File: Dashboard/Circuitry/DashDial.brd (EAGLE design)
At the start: 88.9 x 66.3 mm, 32 parts, among them IC1 TLC5947DAPR, U1 LOGIC SHIFTER, X1 DIAL_IN, X2 SERVO

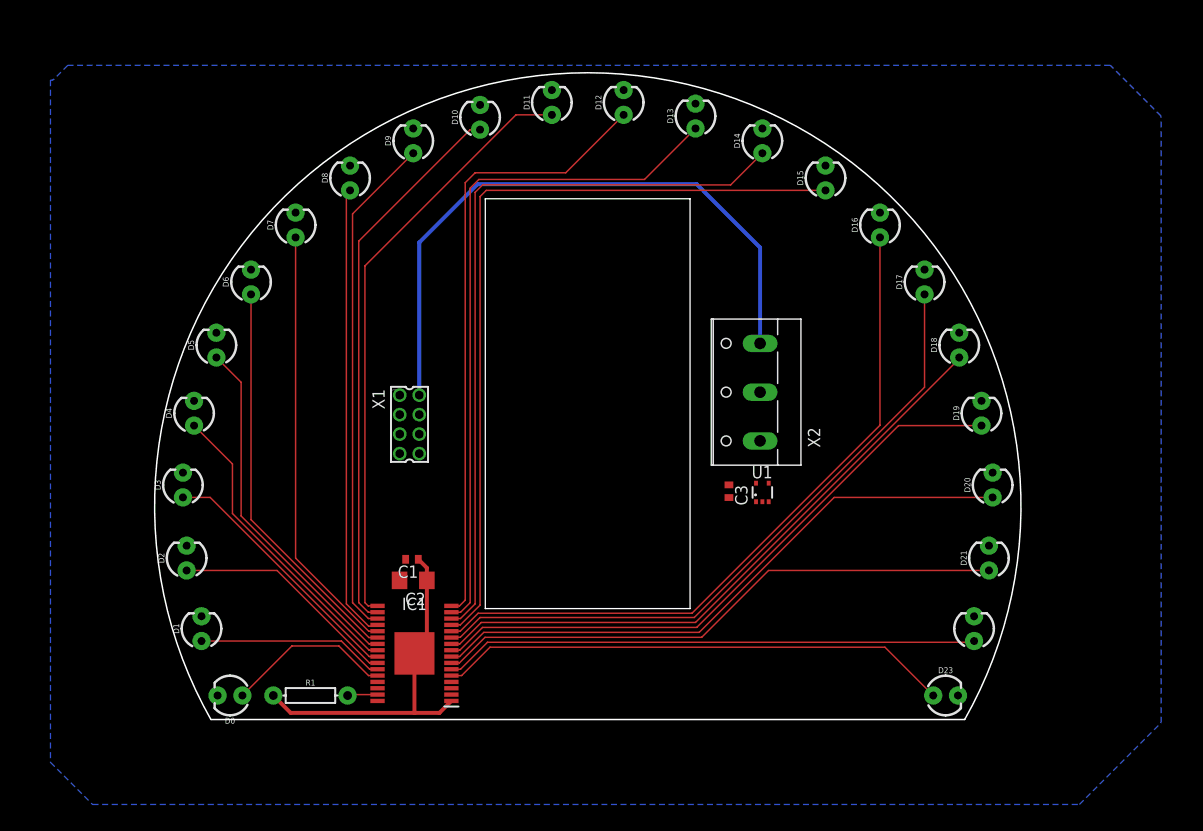
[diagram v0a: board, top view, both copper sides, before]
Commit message: Finished dashboard PCB's! Can send to JLC on Friday. @Andrew
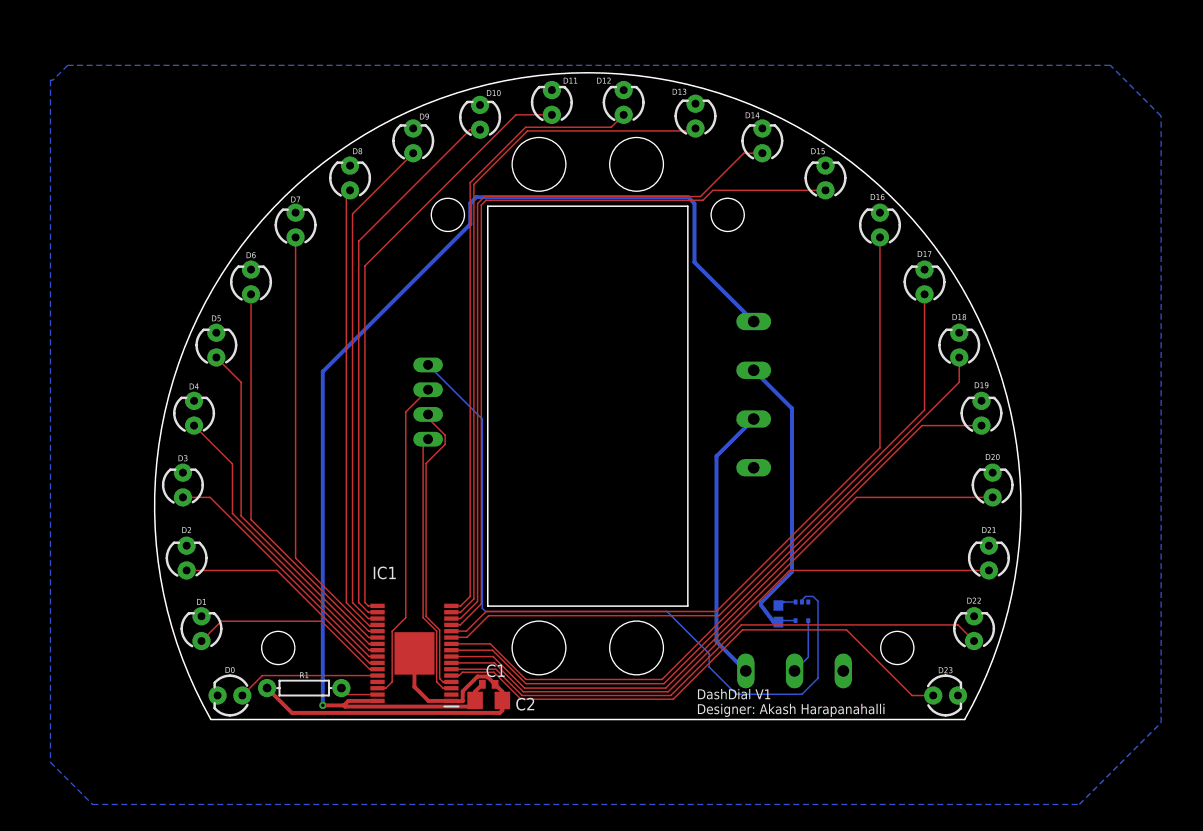
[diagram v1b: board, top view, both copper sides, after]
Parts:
- removed X1: DIAL_IN, con-molex:87758-0816
- added X3: POWER, con-wago-500:W237-4
- added X4: LOGIC, Rembrandt Electronics - JST XH Connectors v1-0:JST-XH-04-PACKAGE-LONG-PAD
- C3: device rcl:C0402 -> SparkFun-Capacitors:0603
- moved X2 27.7 mm to (21.2, -15.6), flipped to the bottom, turned to 0 degrees
- moved C1 15.1 mm to (-10.2, -18.3)
- moved C2 14.6 mm to (-10.2, -19.9)
- moved C3 13.6 mm to (19.6, -11.0), flipped to the bottom, turned to 90 degrees
- moved U1 12.9 mm to (22.0, -10.8), flipped to the bottom, turned to 180 degrees
- moved R1 0.99 mm to (-29.1, -18.7)
- flipped D22 to the top
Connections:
- net 3.3V: now also X3.4; no longer X1.6
- net 5V: now also X3.3; no longer X1.4
- net 7.4V: now also X3.2; no longer X1.2
- net GND: now also X3.1; no longer X1.8
- net LAT: now also X4.3; no longer X1.5
- net SCLK: now also X4.1; no longer X1.3
- net SERVO_CTRL: now also X4.4; no longer X1.7
- net SIN: now also X4.2; no longer X1.1
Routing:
- net 3.3V: track 0.00 -> 117.5 mm, vias 0 -> 1
- net SERVO_CTRL: track 0.00 -> 76.9 mm
- net 7.4V: track 65.6 -> 28.7 mm
- net LAT: track 0.00 -> 33.3 mm
- net 5V: track 0.00 -> 31.5 mm
- net SIN: track 0.00 -> 30.6 mm
- net SCLK: track 0.00 -> 27.5 mm
- net GND: track 36.2 -> 44.4 mm
- net N$1: track 0.00 -> 5.75 mm
- net OUT5: track 63.9 -> 68.8 mm
- net OUT0: track 52.7 -> 56.4 mm
- net OUT1: track 54.8 -> 58.4 mm
- net OUT4: track 63.9 -> 66.8 mm
- net OUT3: track 62.3 -> 65.0 mm
- net OUT23: track 17.2 -> 14.7 mm
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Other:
- outline, holes or cut-outs redrawn
- board text added: "DashDial V1 Designer: Akash Harapanahalli"

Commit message: Finished redesign of DashDial
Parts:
- removed X4: LOGIC, Rembrandt Electronics - JST XH Connectors v1-0:JST-XH-04-PACKAGE-LONG-PAD
- added X1: LOGIC, con-wago-500:W237-4
- moved C2 18.3 mm to (-28.4, -19.3), turned to 0 degrees
- moved C1 15.2 mm to (-25.3, -20.2), turned to 90 degrees
- moved R1 8.66 mm to (-26.9, -10.3), turned to 270 degrees
- moved U1 3.45 mm to (25.3, -9.78)
- moved X3 3.05 mm to (15.2, 11.4), turned to 270 degrees
- moved C3 2.90 mm to (22.1, -9.65)
- moved D10 0.13 mm to (-11.0, 40.0), turned to 270 degrees
- turned D0 to 0 degrees
- turned D1 to 270 degrees
- turned D11 to 270 degrees
- turned D12 to 270 degrees
- turned D13 to 270 degrees
- turned D14 to 270 degrees
- turned D15 to 270 degrees
- turned D16 to 270 degrees
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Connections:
- net 3.3V: now also D0.A, D1.A, D10.A, D11.A, D12.A, D13.A, D14.A, D15.A, D16.A, D17.A, D18.A, D19.A, D2.A, D20.A, D21.A, D22.A, D23.A, D3.A, D4.A, D5.A, D6.A, D7.A, D8.A, D9.A, X3.1; no longer X3.4
- net 5V: now also X3.2; no longer X3.3
- net 7.4V: now also X3.3; no longer X3.2
- net GND: now also IC1.2, X3.4; no longer D0.K, D1.K, D10.K, D11.K, D12.K, D13.K, D14.K, D15.K, D16.K, D17.K, D18.K, D19.K, D2.K, D20.K, D21.K, D22.K, D23.K, D3.K, D4.K, D5.K, D6.K, D7.K, D8.K, D9.K, X3.1
- net LAT: now also X1.3; no longer X4.3
- net OUT0: now also D23.K; no longer D23.A
- net OUT1: now also D22.K; no longer D22.A
- net OUT10: now also D13.K; no longer D13.A
- net OUT11: now also D12.K; no longer D12.A
- net OUT12: now also D11.K; no longer D11.A
- net OUT13: now also D10.K; no longer D10.A
- net OUT14: now also D9.K; no longer D9.A
- net OUT15: now also D8.K; no longer D8.A
- net OUT16: now also D7.K; no longer D7.A
- net OUT17: now also D6.K; no longer D6.A
- net OUT18: now also D5.K; no longer D5.A
- net OUT19: now also D4.K; no longer D4.A
- net OUT2: now also D21.K; no longer D21.A
- net OUT20: now also D3.K; no longer D3.A
- net OUT21: now also D2.K; no longer D2.A
- net OUT22: now also D1.K; no longer D1.A
- net OUT23: now also D0.K; no longer D0.A
- net OUT3: now also D20.K; no longer D20.A
- net OUT4: now also D19.K; no longer D19.A
- net OUT5: now also D18.K; no longer D18.A
- net OUT6: now also D17.K; no longer D17.A
- net OUT7: now also D16.K; no longer D16.A
- net OUT8: now also D15.K; no longer D15.A
- net OUT9: now also D14.K; no longer D14.A
- net SCLK: now also X1.1; no longer X4.1
- net SERVO_CTRL: now also X1.4; no longer X4.4
- net SIN: now also X1.2; no longer X4.2
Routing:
- net 3.3V: track 117.5 -> 21.3 mm, vias 1 -> 0
- net SERVO_CTRL: track 76.9 -> 83.3 mm
- net N$32: track 3.98 -> 8.05 mm, vias 0 -> 1
- net GND: track 44.4 -> 48.0 mm
- net SCLK: track 27.5 -> 24.5 mm
- net N$1: track 5.75 -> 8.13 mm
- net LAT: track 33.3 -> 35.5 mm
- net 5V: track 31.5 -> 29.4 mm
- net SIN: track 30.6 -> 29.3 mm
- added copper zone on layer 16, net 3.3V
- added copper zone on layer 1, net GND
- removed copper zone on layer 16, net GND
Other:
- board text added: "+"
- board text added: "3.3V"
- board text added: "5V"
- board text added: "7.4V"
- board text added: "CTRL"
- board text added: "DashDial V2 Designer: Akash Harapanahalli"
- board text added: "GND"
- board text added: "LAT"
- board text added: "SCLK"
- board text added: "SIN"
- board text removed: "DashDial V1 Designer: Akash Harapanahalli"

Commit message: Actually finished DashDial this time :)
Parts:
- removed X1: LOGIC, con-wago-500:W237-4
- removed X3: POWER, con-wago-500:W237-4
- added J1, J2: ESW-104-23-L-D, ESW-104-23-L-D:SAMTEC_ESW-104-23-L-D
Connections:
- net 3.3V: now also J1.07, J2.07; no longer X3.1
- net 5V: now also J1.05, J2.05; no longer X3.2
- net 7.4V: now also J1.03, J2.03; no longer X3.3
- net GND: now also J1.01, J2.01; no longer X3.4
- net LAT: now also J1.04, J2.04; no longer X1.3
- net SCLK: now also J1.08, J2.08; no longer X1.1
- net SERVO_CTRL: now also J1.02, J2.02; no longer X1.4
- net SIN: now also J1.06, J2.06; no longer X1.2
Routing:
- net 5V: track 29.4 -> 144.3 mm, vias 0 -> 4
- net GND: track 48.0 -> 129.6 mm
- net SCLK: track 24.5 -> 105.8 mm, vias 0 -> 1
- net SIN: track 29.3 -> 107.0 mm, vias 0 -> 1
- net 7.4V: track 28.6 -> 103.5 mm
- net LAT: track 35.5 -> 101.8 mm, vias 0 -> 1
- net SERVO_CTRL: track 83.3 -> 147.3 mm, vias 0 -> 4
- net OUT20: track 26.7 -> 37.6 mm
- net OUT3: track 65.0 -> 70.1 mm
- net OUT19: track 31.3 -> 34.7 mm
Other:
- board text removed: "3.3V"
- board text removed: "5V"
- board text removed: "LAT"
- board text removed: "SCLK"
- board text removed: "SIN"

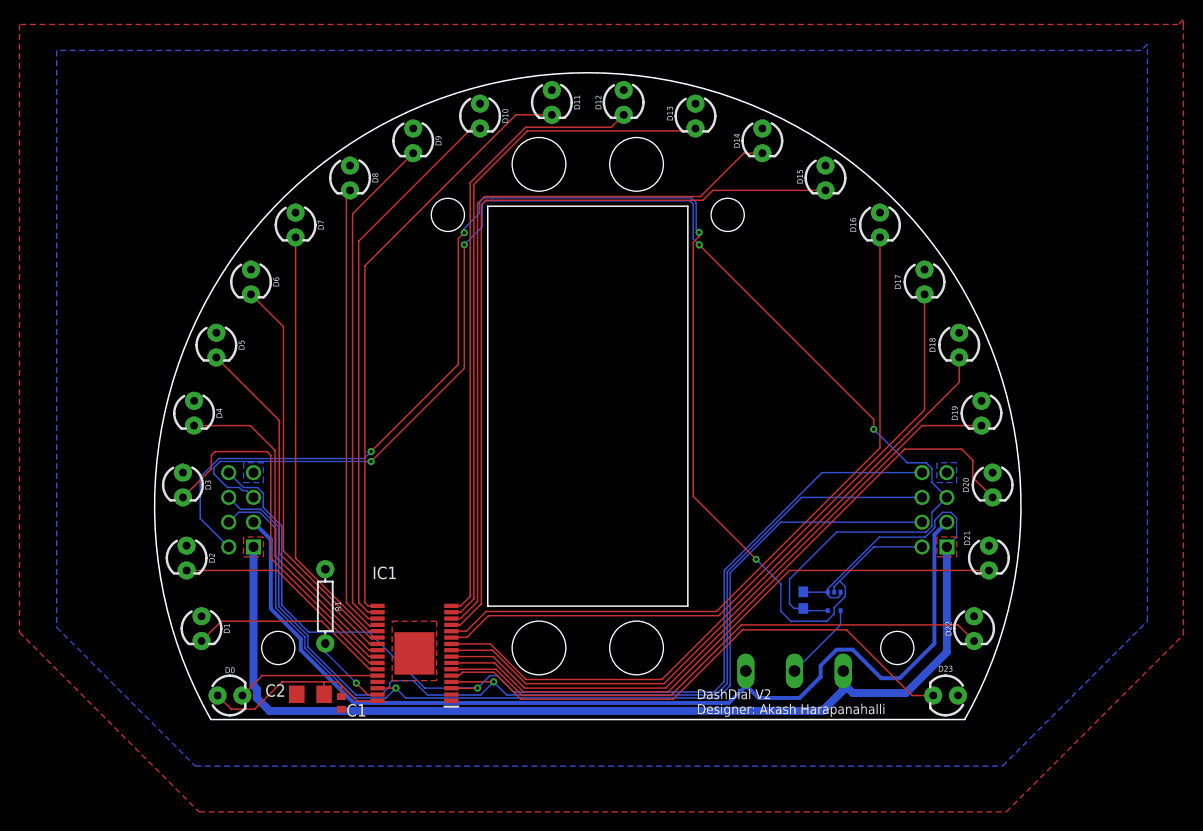
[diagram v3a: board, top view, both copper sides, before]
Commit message: Finished DashDial and DashHub redesign, very rushed.
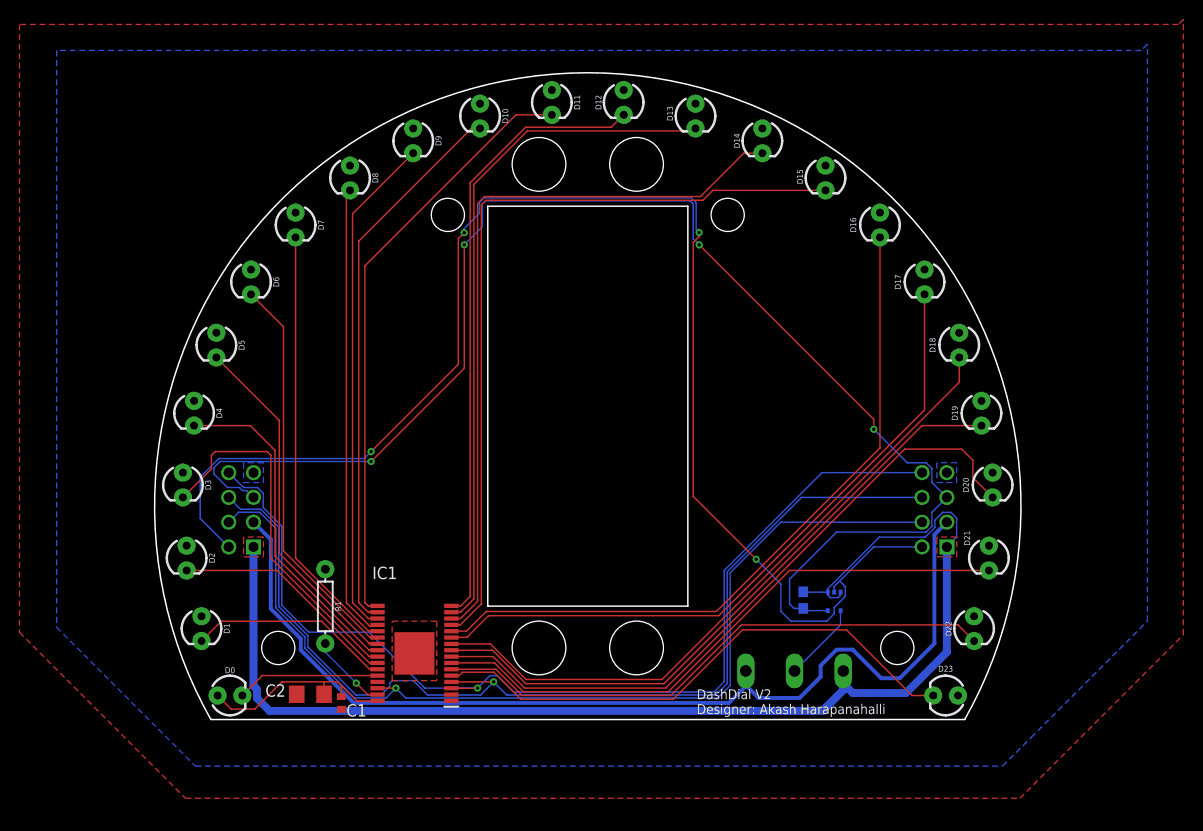
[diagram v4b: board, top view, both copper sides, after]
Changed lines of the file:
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@@
 <vertex x="-58.293" y="49.403"/>
 <vertex x="-58.293" y="-12.954"/>
-<vertex x="-39.878" y="-31.369"/>
-<vertex x="42.926" y="-31.369"/>
+<vertex x="-41.275" y="-29.972"/>
+<vertex x="44.323" y="-29.972"/>
 <vertex x="61.087" y="-13.208"/>
-<vertex x="61.087" y="49.149"/>
 <vertex x="61.087" y="49.911"/>
 <vertex x="60.579" y="49.403"/>
